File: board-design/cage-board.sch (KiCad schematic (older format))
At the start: 48 parts, among them J1 Jack-DC, J10 73131-0240, J11 73131-0240, J12 73131-0240, J13 Conn_01x02, J14 Conn_01x02, J2 Conn_02x17_Ribbon, J3 TB002-500-03BE, J4 73131-0240, J5 73131-0240, J6 73131-0240, J7 TB002-500-03BE, J8 73131-0240, J9 TB002-500-03BE, Q1 BD139, Q2 BD139, U1 74LS06, U3 ERJ-UP8F6200V, U4 ERJ-UP8F6200V

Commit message: Add USB board with 3D
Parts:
- removed H1, H2, H3: MountingHole, MountingHole:MountingHole_3.2mm_M3, symbol Mechanical:MountingHole
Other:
- note removed: "double check the footprint on these\n"
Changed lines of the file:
@@
 NoConn ~ 8800 1400
-$Comp
-L Mechanical:MountingHole H1
-U 1 1 5F9D4D8C
-P 8050 5425
-F 0 "H1" H 8150 5471 50  0000 L CNN
-F 1 "MountingHole" H 8150 5380 50  0000 L CNN
-F 2 "MountingHole:MountingHole_3.2mm_M3" H 8050 5425 50  0001 C CNN
-F 3 "~" H 8050 5425 50  0001 C CNN
-	1    8050 5425
-	1    0    0    -1
-$EndComp
-$Comp
-L Mechanical:MountingHole H2
-U 1 1 5F9E1E25
-P 8100 5075
-F 0 "H2" H 8200 5121 50  0000 L CNN
-F 1 "MountingHole" H 8200 5030 50  0000 L CNN
-F 2 "MountingHole:MountingHole_3.2mm_M3" H 8100 5075 50  0001 C CNN
-F 3 "~" H 8100 5075 50  0001 C CNN
-	1    8100 5075
-	1    0    0    -1
-$EndComp
-$Comp
-L Mechanical:MountingHole H3
-U 1 1 5F9E1F41
-P 8400 5300
-F 0 "H3" H 8500 5346 50  0000 L CNN
-F 1 "MountingHole" H 8500 5255 50  0000 L CNN
-F 2 "MountingHole:MountingHole_3.2mm_M3" H 8400 5300 50  0001 C CNN
-F 3 "~" H 8400 5300 50  0001 C CNN
-	1    8400 5300
-	1    0    0    -1
-$EndComp
-Text Notes 7850 5650 0    50   ~ 0
-double check the footprint on these\n
 $Comp
 L Device:D_Small D2

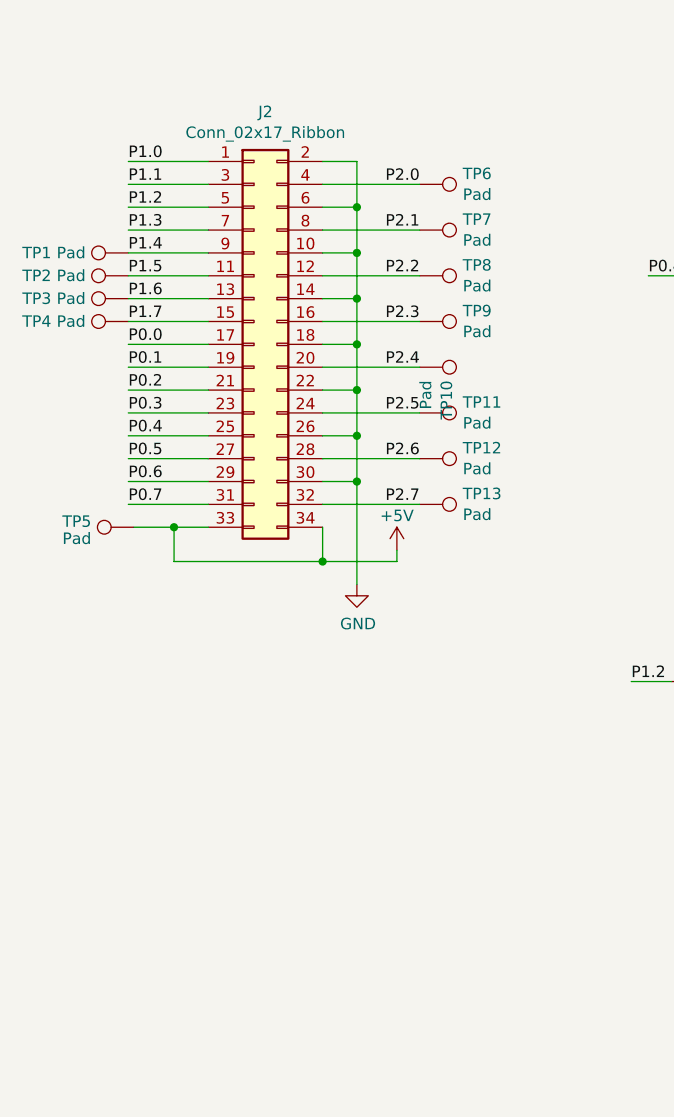
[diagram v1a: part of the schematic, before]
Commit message: moved screw terminals and updated test points
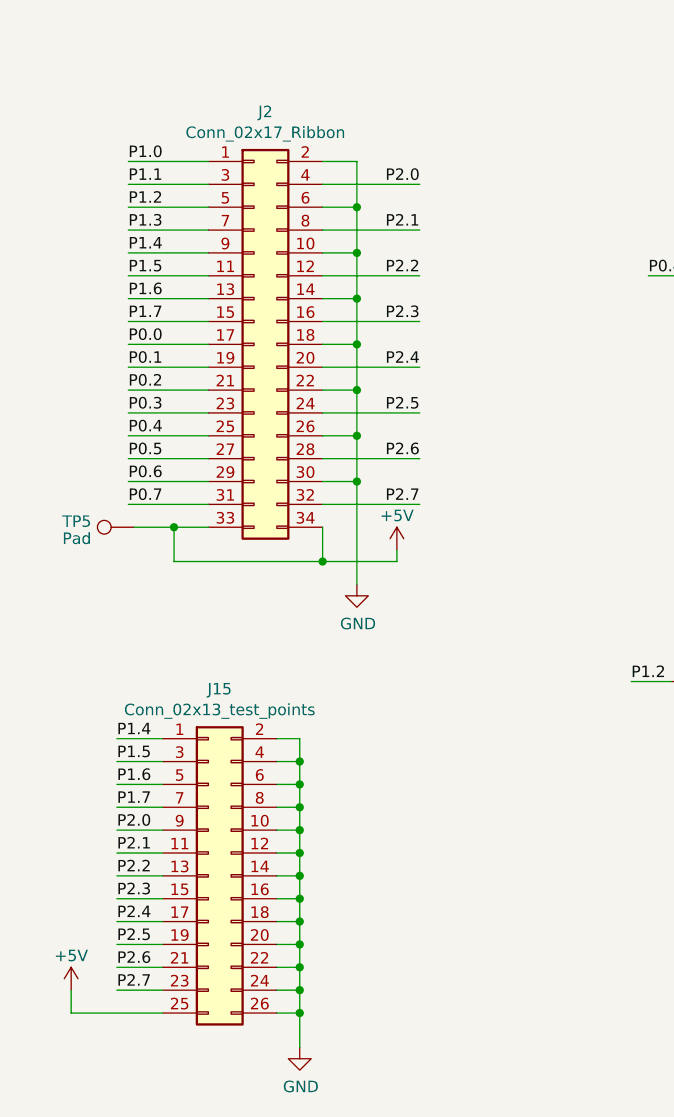
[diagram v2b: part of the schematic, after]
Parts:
- removed TP1, TP10, TP11, TP12, TP13, TP2, TP3, TP4, TP6, TP7, TP8, TP9: Pad, TestPoint:TestPoint_Pad_4.0x4.0mm, symbol Connector:TestPoint
- added J15: Conn_02x13_test_points, Connector_PinHeader_2.54mm:PinHeader_2x13_P2.54mm_Vertical, symbol Connector_Generic:Conn_02x13_Odd_Even
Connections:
- net +5V: now also J15.25 (Pin_25)
- net GND: now also J15.10 (Pin_10), J15.12 (Pin_12), J15.14 (Pin_14), J15.16 (Pin_16), J15.18 (Pin_18), J15.2 (Pin_2), J15.20 (Pin_20), J15.22 (Pin_22), J15.24 (Pin_24), J15.26 (Pin_26), J15.4 (Pin_4), J15.6 (Pin_6), J15.8 (Pin_8)
- net P1.4: now also J15.1 (Pin_1)
- net P1.5: now also J15.3 (Pin_3)
- net P1.6: now also J15.5 (Pin_5)
- net P1.7: now also J15.7 (Pin_7)
- net P2.0: now also J15.9 (Pin_9)
- net P2.1: now also J15.11 (Pin_11)
- net P2.2: now also J15.13 (Pin_13)
- net P2.3: now also J15.15 (Pin_15)
- net P2.4: now also J15.17 (Pin_17)
- net P2.5: now also J15.19 (Pin_19)
- net P2.6: now also J15.21 (Pin_21)
- net P2.7: now also J15.23 (Pin_23)

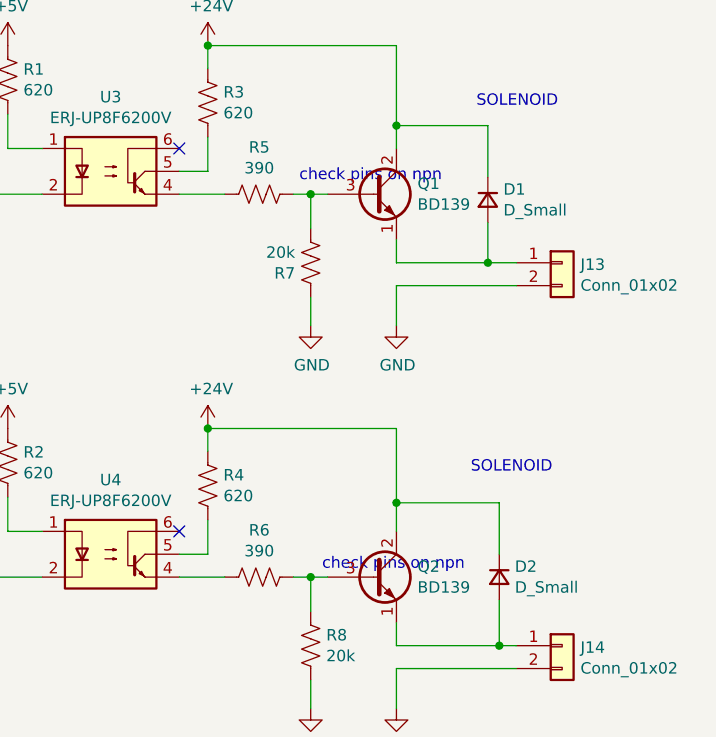
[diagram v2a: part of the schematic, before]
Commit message: fixing schematic notes
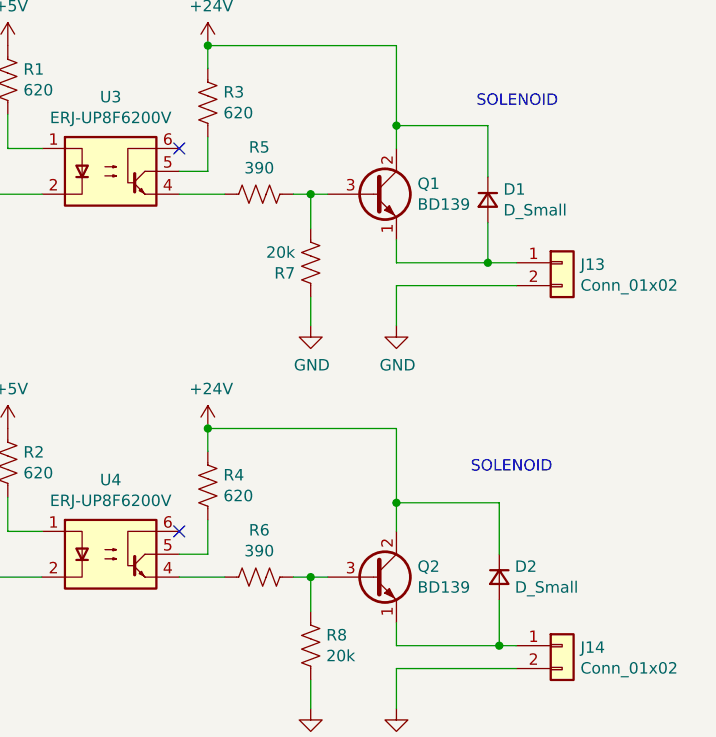
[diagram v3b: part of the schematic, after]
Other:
- note removed: "check pins on npn"
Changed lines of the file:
@@
 	1200 1400 1200 1500
 Connection ~ 1200 1500
-Text Notes 9325 1550 0    50   ~ 0
-check pins on npn
 $Comp
 L Device:R_US R7
@@
 	1    0    0    -1
 $EndComp
-Text Notes 9425 3250 0    50   ~ 0
-check pins on npn
 $Comp
 L Connector:TestPoint TP5

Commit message: fixing 3d models hopefully
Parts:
- removed TP5: Pad, TestPoint:TestPoint_Pad_4.0x4.0mm, symbol Connector:TestPoint
- U1: Item Cost (none) -> 0.99; ItemCost 0.99 -> (none)
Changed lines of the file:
@@
 F 5 "296-3623-5-ND" H 3725 5350 50  0001 C CNN "Supplier P/N"
 F 6 "SN74LS06D" H 3725 5350 50  0001 C CNN "MFN"
-F 7 "0.99" H 3725 5350 50  0001 C CNN "ItemCost"
+F 7 "0.99" H 3725 5350 50  0001 C CNN "Item Cost"
 	3    3725 5350
 	1    0    0    -1
@@
 	1    0    0    -1
 $EndComp
-$Comp
-L Connector:TestPoint TP5
-U 1 1 5F74AE16
-P 1075 4675
-F 0 "TP5" V 1100 4925 50  0000 C CNN
-F 1 "Pad" V 1025 4925 50  0000 C CNN
-F 2 "TestPoint:TestPoint_Pad_4.0x4.0mm" H 1275 4675 50  0001 C CNN
-F 3 "~" H 1275 4675 50  0001 C CNN
-	1    1075 4675
-	0    -1   -1   0
-$EndComp
 Wire Wire Line
 	2050 4475 2050 4925
@@
 	1    0    0    -1
 $EndComp
-Wire Wire Line
-	1075 4675 1250 4675
 $Comp
 L power:+5V #PWR0127
@@
 	1250 4825 1250 4675
 Connection ~ 1900 4825
-Connection ~ 1250 4675
 Wire Wire Line
 	1250 4675 1400 4675

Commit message: Rev B mods
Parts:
- removed unit 3 of U1
- removed unit 4 of U1
- removed unit 5 of U1
- removed unit 6 of U1
- added D? (x2): 1N4007, Diode_THT:D_DO-41_SOD81_P10.16mm_Horizontal, symbol Diode:1N4007
- added Q? (x2): 2N3906, Package_TO_SOT_THT:TO-92_Inline, symbol Transistor_BJT:2N3906
- added R? (x2): R_US, symbol Device:R_US
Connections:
- net +5V: now also Q?.1 (E), Q?.1 (E)
- net GND: now also D?.2 (A), D?.2 (A)
- net P1.0: now also U3.2
- net P1.1: now also U4.2
- net P1.2: now also R?.2
- net P1.3: now also R?.2
- net at J5.1 (In): now also D?.1 (K), Q?.3 (C)
- net at J11.1 (In): now also D?.1 (K), Q?.3 (C)
- new net: Q?.2 (B), R?.1 (x2)
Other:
- note added: "B"
- note added: "Boston University Electronics Design Facility"
- note added: "Chen Lab cage board"
- note added: "Rev B changes:\nOmit inverter on air solenoid drive\nAdd drive circuit on water solenoids\nAdd DC/DC for 5V and some LEDs\nReplace 74LS06 with 74LS04"
- moved on the sheet: J11, J5

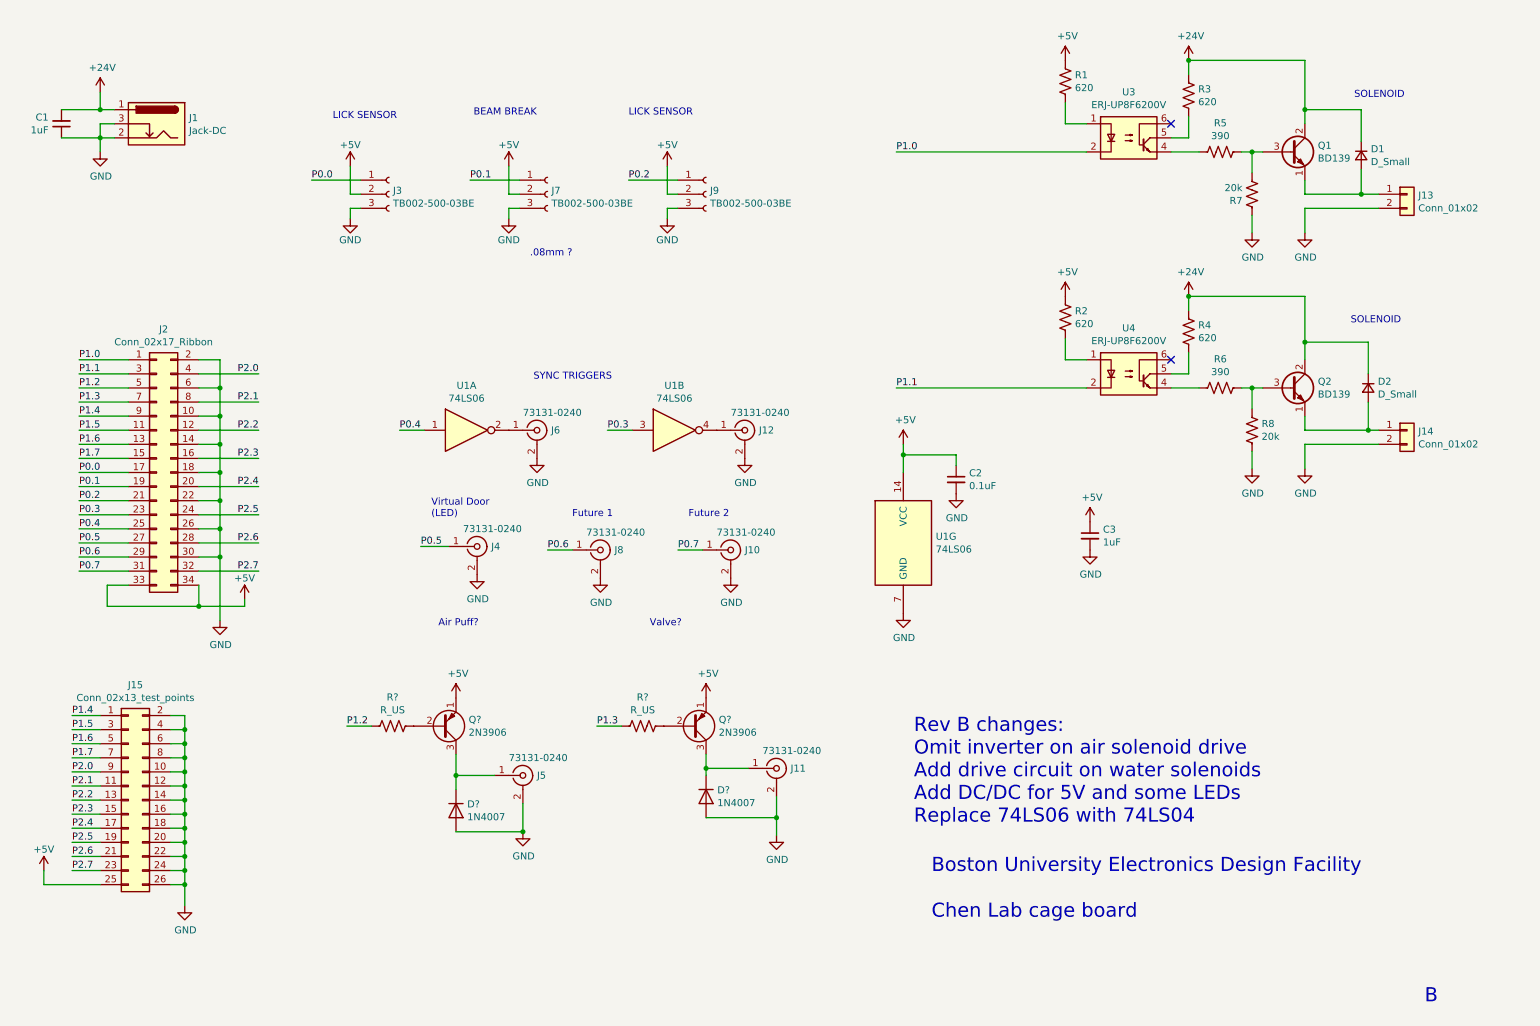
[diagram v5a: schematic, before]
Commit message: Rev B changes to sch done?
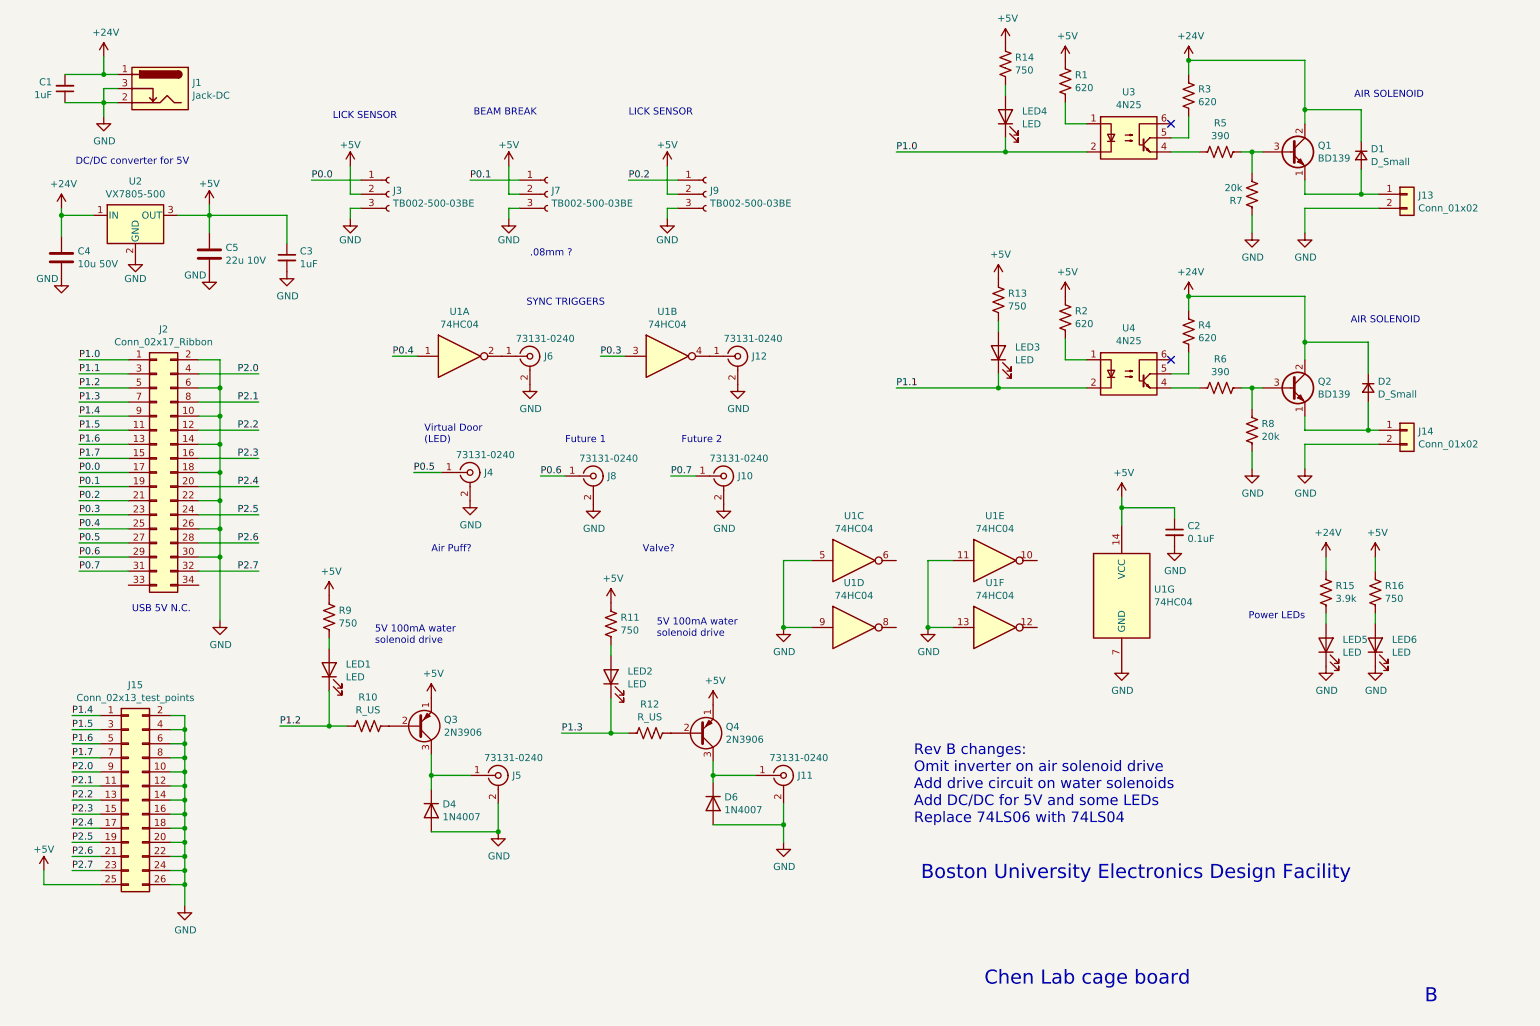
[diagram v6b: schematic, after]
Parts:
- added C4: 10u 50V, symbol Device:C
- added C5: 22u 10V, symbol Device:C
- added LED1, LED2, LED3, LED4, LED5, LED6: LED, LED_THT:LED_D3.0mm, symbol Device:LED
- added R11, R13, R14, R16, R9: 750, symbol Device:R_US
- added R15: 3.9k, symbol Device:R_US
- added unit 3 of U1
- added unit 4 of U1
- added unit 5 of U1
- added unit 6 of U1
- added U2: VX7805-500, Package_TO_SOT_THT:TO-220-3_Vertical, symbol Regulator_Linear:uA7805
- D4, D6: renamed from D?; CatNo (none) -> 1497-1491-ND; MFN (none) -> XLUR34D; Supplier (none) -> Digi-Key
- U1: value 74LS06 -> 74HC04
- U3, U4: value ERJ-UP8F6200V -> 4N25
- gave numbers to parts that had none: 4
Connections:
- net +24V: now also C4.1, R15.1, U2.1 (IN)
- net +5V: now also C5.1, R11.1, R13.1, R14.1, R16.1, R9.1, U2.3 (OUT); no longer J2.33 (Pin_33), J2.34 (Pin_34)
- net GND: now also C4.2, C5.2, LED5.1 (K), LED6.1 (K), U1.11, U1.13, U1.5, U1.9, U2.2 (GND)
- net P1.0: now also LED4.1 (K)
- net P1.1: now also LED3.1 (K)
- net P1.2: now also LED1.1 (K)
- net P1.3: now also LED2.1 (K)
- new net: LED5.2 (A), R15.2
- new net: LED6.2 (A), R16.2
- new net: LED3.2 (A), R13.2
- new net: LED4.2 (A), R14.2
- new net: LED1.2 (A), R9.2
- new net: LED2.2 (A), R11.2
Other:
- note added: "5V 100mA water\nsolenoid drive"
- note added: "AIR SOLENOID"
- note added: "DC/DC converter for 5V"
- note added: "Power LEDs"
- note added: "USB 5V N.C."
- note removed: "SOLENOID"
- moved on the sheet: C1, C2, C3, D4, D6, J1, J10, J11, J12, J4, J5, J6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

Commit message: updating schematic, and moving PCB layout forward to RevB
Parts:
- C1, C3: MFN (none) -> C0805C105K5PAC7800
- C4: footprint (none) -> Capacitor_SMD:C_1210_3225Metric_Pad1.33x2.70mm_HandSolder; Item Cost (none) -> 0.94; MFN (none) -> C1210C106K5PAC7210; Supplier (none) -> Digi-Key; Supplier P/N (none) -> 399-C1210C106K5PAC7210CT-ND
- C5: footprint (none) -> Capacitor_SMD:C_0805_2012Metric_Pad1.18x1.45mm_HandSolder; Item Cost (none) -> 0.51; MFN (none) -> C0805C226M8PAC7800; Supplier (none) -> Digi-Key; Supplier P/N (none) -> 399-12069-1-ND
- D4, D6: CatNo 1497-1491-ND -> (none); Item Cost (none) -> 0.31; Supplier P/N (none) -> 1497-1491-ND
- J2: footprint Connector_PinHeader_2.54mm:PinHeader_2x17_P2.54mm_Vertical_SMD -> Connector_PinHeader_2.54mm:PinHeader_2x17_P2.54mm_Vertical; Item Cost 6.14 -> 2.55; MFN N2534-6V0C-RB-WF -> D2534-6002-AR; Supplier P/N MSH34KCT-ND -> MHC34E-ND
- LED1, LED2, LED3, LED4, LED5, LED6: Item Cost (none) -> 0.53; MFN (none) -> LTW-420D7; Supplier (none) -> Digi-Key; Supplier P/N (none) -> 160-1782-ND
- Q3, Q4: Item Cost (none) -> 0.21; MFN (none) -> 2N3906BU; Supplier (none) -> Digi-Key; Supplier P/N (none) -> 2N3906FS-ND
- R10, R12: value R_US -> 1.5k; footprint (none) -> Resistor_SMD:R_0805_2012Metric_Pad1.20x1.40mm_HandSolder; Item Cost (none) -> 0.10; MFN (none) -> RK73B2ATTD152J; Supplier (none) -> Digi-Key; Supplier P/N (none) -> 2019-RK73B2ATTD152JCT-ND
- R11, R13, R14, R16, R9: value 750 -> 200; footprint (none) -> Resistor_SMD:R_0805_2012Metric_Pad1.20x1.40mm_HandSolder; Item Cost (none) -> 0.10; MFN (none) -> RK73B2ATTD201J; Supplier (none) -> Digi-Key; Supplier P/N (none) -> 2019-RK73B2ATTD201JCT-ND
- R15: value 3.9k -> 1k; footprint (none) -> Resistor_SMD:R_0805_2012Metric_Pad1.20x1.40mm_HandSolder; Item Cost (none) -> 0.10; MFN (none) -> RK73B2ATTD102J; Supplier (none) -> Digi-Key; Supplier P/N (none) -> 2019-RK73B2ATTD102JCT-ND
- U1: footprint Package_SO:SOIC-14_3.9x8.7mm_P1.27mm -> Package_DIP:DIP-14_W7.62mm_Socket_LongPads; Item Cost 0.99 -> 0.73; MFN SN74LS06D -> SN74LS04N; Supplier P/N 296-3623-5-ND -> 296-1629-5-ND
- U2: CatNo 102-4244-ND -> (none); Item Cost (none) -> 2.78; Supplier (none) -> Digi-Key; Supplier P/N (none) -> 102-4244-ND
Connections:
- no-connect marks 2 -> 4

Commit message: auto push run at Fri Apr  9 11:10:50 EDT 2021
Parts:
- added J16, J17, J18: TB002-500-03BE, TerminalBlock:TerminalBlock_bornier-3_P5.08mm, symbol Connector:Conn_01x03_Female
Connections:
- net +5V: now also J16.2 (Pin_2), J17.2 (Pin_2), J18.2 (Pin_2)
- net GND: now also J16.3 (Pin_3), J17.3 (Pin_3), J18.3 (Pin_3)
- net P2.0: now also J16.1 (Pin_1)
- net P2.1: now also J17.1 (Pin_1)
- net P2.2: now also J18.1 (Pin_1)
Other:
- moved on the sheet: D4, D6, J10, J11, J12, J3, J4, J5, J6, J7, J8, J9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
